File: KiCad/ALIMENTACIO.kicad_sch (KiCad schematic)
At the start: 17 parts, among them J1 Conn_01x02_Pin, U1 LM2596S-5, U2 LM1117DT-3.3

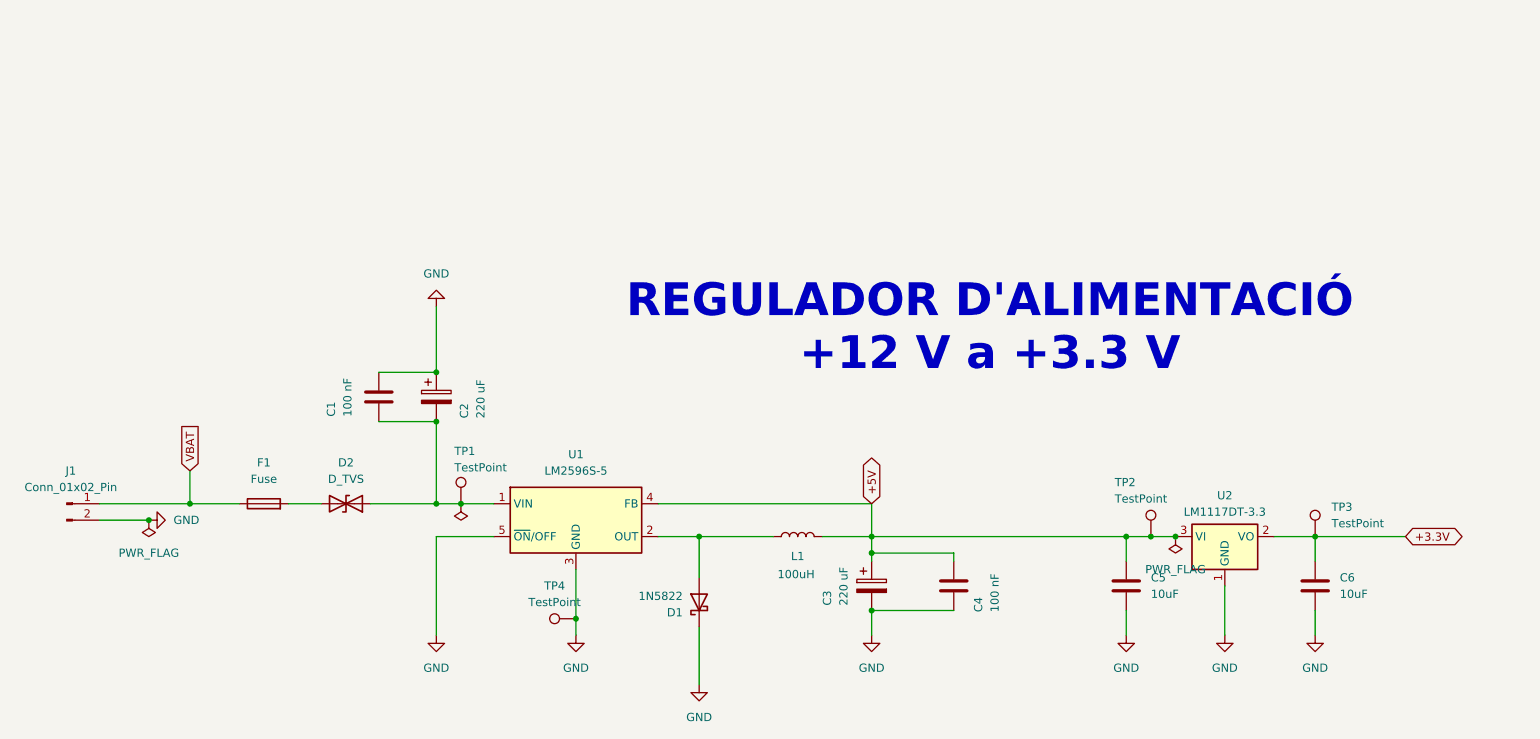
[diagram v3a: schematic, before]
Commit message: Modificació d'errors varis
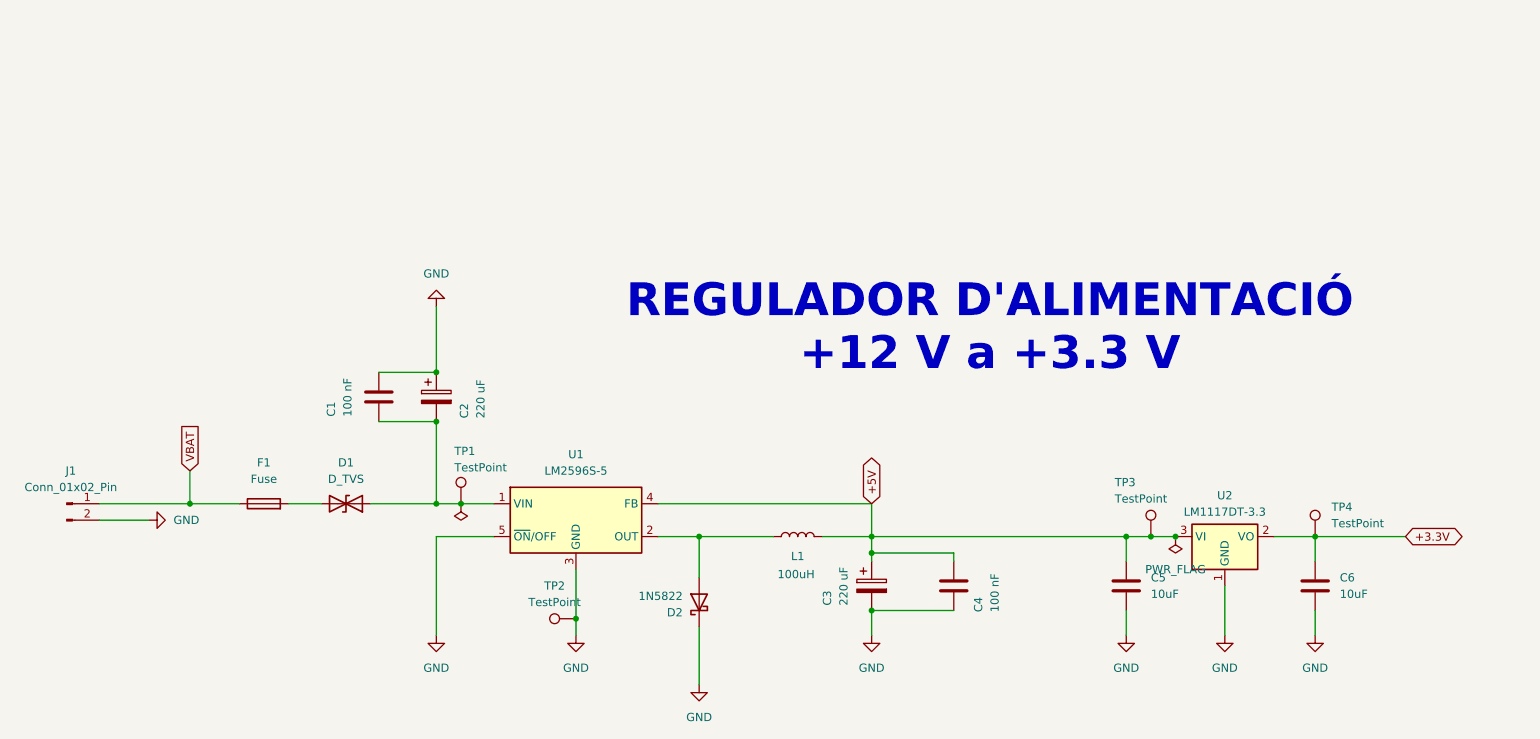
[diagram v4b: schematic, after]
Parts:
- renumbered D2 to D1, D1 to D2, TP4 to TP2, TP2 to TP3, TP3 to TP4
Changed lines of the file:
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@@
-	)
-	(junction
-		(at 55.88 109.22)
-		(diameter 0)
-		(color 0 0 0 0)
 	)
 	(junction
@@
 		(dnp no)
 		(fields_autoplaced yes)
-		(property "Reference" "TP4"
+		(property "Reference" "TP2"
 			(at 118.618 119.38 90)
 			(effects
@@
 		(dnp no)
 		(fields_autoplaced yes)
-		(property "Reference" "D2"
+		(property "Reference" "D1"
 			(at 86.36 100.33 0)
 			(effects
@@
 		(dnp no)
 		(fields_autoplaced yes)
-		(property "Reference" "TP3"
+		(property "Reference" "TP4"
 			(at 238.76 107.1879 0)
 			(effects
@@
 		(dnp no)
 		(fields_autoplaced yes)
-		(property "Reference" "#PWR05"
+		(property "Reference" "#PWR06"
 			(at 167.64 133.35 0)
 			(effects
@@
 		(dnp no)
 		(fields_autoplaced yes)
-		(property "Reference" "D1"
+		(property "Reference" "D2"
 			(at 138.43 123.5076 90)
 			(effects
@@
 		(dnp no)
 		(fields_autoplaced yes)
-		(property "Reference" "#PWR02"
+		(property "Reference" "#PWR03"
 			(at 100.33 133.35 0)
 			(effects
@@
 		(dnp no)
 		(fields_autoplaced yes)
-		(property "Reference" "#PWR08"
+		(property "Reference" "#PWR09"
 			(at 236.22 133.35 0)
 			(effects
@@
 		(dnp no)
 		(fields_autoplaced yes)
-		(property "Reference" "#PWR07"
+		(property "Reference" "#PWR08"
 			(at 222.25 133.35 0)
 			(effects
@@
 		(dnp no)
 		(fields_autoplaced yes)
-		(property "Reference" "#PWR03"
+		(property "Reference" "#PWR04"
 			(at 121.92 133.35 0)
 			(effects
@@
 		(on_board yes)
 		(dnp no)
-		(property "Reference" "TP2"
+		(property "Reference" "TP3"
 			(at 205.232 103.378 0)
 			(effects
@@
 		(dnp no)
 		(fields_autoplaced yes)
-		(property "Reference" "#PWR06"
+		(property "Reference" "#PWR07"
 			(at 207.01 133.35 0)
 			(effects
@@
 		(dnp no)
 		(fields_autoplaced yes)
-		(property "Reference" "#FLG03"
+		(property "Reference" "#FLG0104"
 			(at 214.63 113.665 0)
 			(effects
@@
 				)
 			)
+			(project "SEIENTS_EDD"
+				(path "/b6401b4f-5426-49b8-bb2e-8ecdb19989ef/67d546eb-b5d9-4a2c-a3ee-41df96785a31"
+					(reference "#FLG0104")
+					(unit 1)
+				)
+			)
 		)
 	)
@@
 		(dnp no)
 		(fields_autoplaced yes)
-		(property "Reference" "#PWR04"
+		(property "Reference" "#PWR05"
 			(at 140.97 140.97 0)
 			(effects
@@
 	(symbol
 		(lib_id "power:PWR_FLAG")
-		(at 55.88 109.22 180)
+		(at 104.14 106.68 180)
 		(unit 1)
 		(exclude_from_sim no)
@@
 		(dnp no)
 		(fields_autoplaced yes)
-		(property "Reference" "#FLG02"
-			(at 55.88 111.125 0)
-			(effects
-				(font
-					(size 1.27 1.27)
-				)
-				(hide yes)
-			)
-		)
-		(property "Value" "PWR_FLAG"
-			(at 55.88 114.3 0)
-			(effects
-				(font
-					(size 1.27 1.27)
-				)
-			)
-		)
-		(property "Footprint" ""
-			(at 55.88 109.22 0)
-			(effects
-				(font
-					(size 1.27 1.27)
-				)
-				(hide yes)
-			)
-		)
-		(property "Datasheet" "~"
-			(at 55.88 109.22 0)
-			(effects
-				(font
-					(size 1.27 1.27)
-				)
-				(hide yes)
-			)
-		)
-		(property "Description" "Special symbol for telling ERC where power comes from"
-			(at 55.88 109.22 0)
-			(effects
-				(font
-					(size 1.27 1.27)
-				)
-				(hide yes)
-			)
-		)
-		(pin "1"
-		)
-		(instances
-			(project ""
-				(path "/45cfcaa5-e694-40cb-923c-70f0cad76365"
-					(reference "#FLG02")
-					(unit 1)
-				)
-			)
-		)
-	)
-	(symbol
-		(lib_id "power:PWR_FLAG")
-		(at 104.14 106.68 180)
-		(unit 1)
-		(exclude_from_sim no)
-		(in_bom yes)
-		(on_board yes)
-		(dnp no)
-		(fields_autoplaced yes)
-		(property "Reference" "#FLG01"
+		(property "Reference" "#FLG03"
 			(at 104.14 108.585 0)
 			(effects
@@
 		(dnp no)
 		(fields_autoplaced yes)
-		(property "Reference" "#PWR09"
+		(property "Reference" "#PWR02"
 			(at 100.33 69.85 0)
 			(effects

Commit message: cambios en organizacion
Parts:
- renumbered D2 to D1, D1 to D2, TP3 to TP2, TP4 to TP3, TP2 to TP4
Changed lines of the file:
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@@
 	(text "REGULADOR D'ALIMENTACIÓ\n+12 V a +3.3 V"
 		(exclude_from_sim no)
-		(at 185.928 79.502 0)
+		(at 138.684 53.848 0)
 		(effects
 			(font
+				(face "Arial Black")
 				(size 5.08 5.08)
 				(thickness 0.254)
@@
 		(dnp no)
 		(fields_autoplaced yes)
-		(property "Reference" "TP2"
+		(property "Reference" "TP4"
 			(at 118.618 119.38 90)
 			(effects
@@
 		(dnp no)
 		(fields_autoplaced yes)
-		(property "Reference" "D1"
+		(property "Reference" "D2"
 			(at 86.36 100.33 0)
 			(effects
@@
 		(dnp no)
 		(fields_autoplaced yes)
-		(property "Reference" "TP4"
+		(property "Reference" "TP3"
 			(at 238.76 107.1879 0)
 			(effects
@@
 		(dnp no)
 		(fields_autoplaced yes)
-		(property "Reference" "#PWR06"
+		(property "Reference" "#PWR05"
 			(at 167.64 133.35 0)
 			(effects
@@
 		(dnp no)
 		(fields_autoplaced yes)
-		(property "Reference" "D2"
+		(property "Reference" "D1"
 			(at 138.43 123.5076 90)
 			(effects
@@
 		(dnp no)
 		(fields_autoplaced yes)
-		(property "Reference" "#PWR03"
+		(property "Reference" "#PWR02"
 			(at 100.33 133.35 0)
 			(effects
@@
 		(dnp no)
 		(fields_autoplaced yes)
-		(property "Reference" "#PWR09"
+		(property "Reference" "#PWR08"
 			(at 236.22 133.35 0)
 			(effects
@@
 		(dnp no)
 		(fields_autoplaced yes)
-		(property "Reference" "#PWR08"
+		(property "Reference" "#PWR07"
 			(at 222.25 133.35 0)
 			(effects
@@
 		(dnp no)
 		(fields_autoplaced yes)
-		(property "Reference" "#PWR04"
+		(property "Reference" "#PWR03"
 			(at 121.92 133.35 0)
 			(effects
@@
 		(on_board yes)
 		(dnp no)
-		(property "Reference" "TP3"
+		(property "Reference" "TP2"
 			(at 205.232 103.378 0)
 			(effects
@@
 		(dnp no)
 		(fields_autoplaced yes)
-		(property "Reference" "#PWR07"
+		(property "Reference" "#PWR06"
 			(at 207.01 133.35 0)
 			(effects
@@
 		(dnp no)
 		(fields_autoplaced yes)
-		(property "Reference" "#FLG0104"
+		(property "Reference" "#FLG03"
 			(at 214.63 113.665 0)
 			(effects
@@
 		(dnp no)
 		(fields_autoplaced yes)
-		(property "Reference" "#PWR05"
+		(property "Reference" "#PWR04"
 			(at 140.97 140.97 0)
 			(effects
@@
 		(dnp no)
 		(fields_autoplaced yes)
-		(property "Reference" "#FLG03"
+		(property "Reference" "#FLG01"
 			(at 104.14 108.585 0)
 			(effects
@@
 		(dnp no)
 		(fields_autoplaced yes)
-		(property "Reference" "#PWR02"
+		(property "Reference" "#PWR09"
 			(at 100.33 69.85 0)
 			(effects

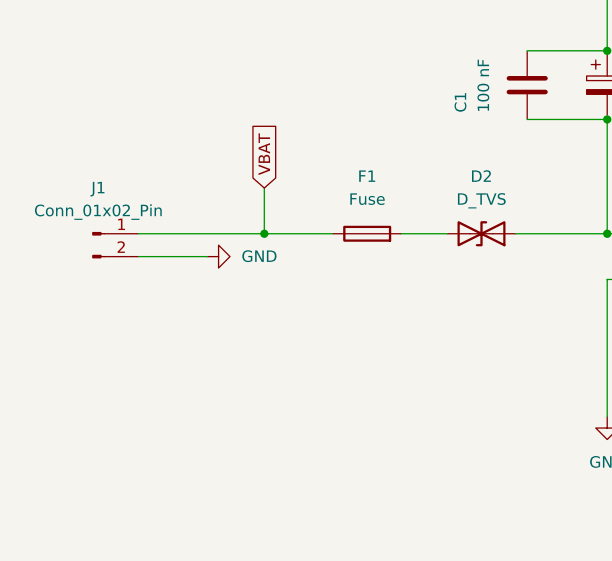
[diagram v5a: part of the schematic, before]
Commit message: Modificació d'errors varis
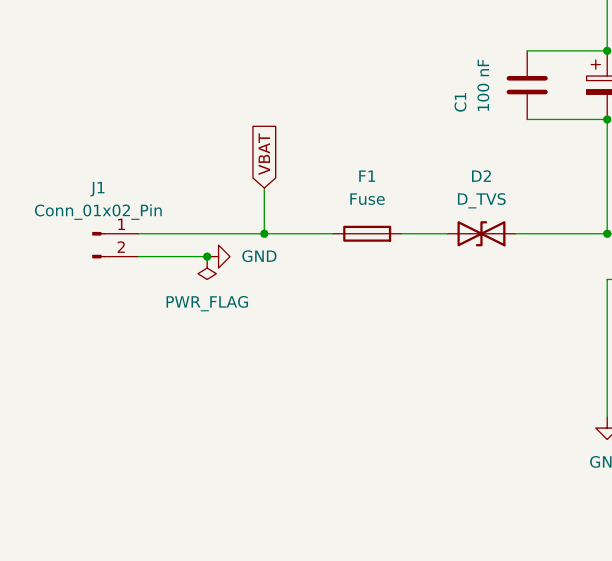
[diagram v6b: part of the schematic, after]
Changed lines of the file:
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@@
+	)
+	(junction
+		(at 55.88 109.22)
+		(diameter 0)
+		(color 0 0 0 0)
 	)
 	(junction
@@
 					(unit 1)
 				)
+			)
+		)
+	)
+	(symbol
+		(lib_id "power:PWR_FLAG")
+		(at 55.88 109.22 180)
+		(unit 1)
+		(exclude_from_sim no)
+		(in_bom yes)
+		(on_board yes)
+		(dnp no)
+		(fields_autoplaced yes)
+		(property "Reference" "#FLG02"
+			(at 55.88 111.125 0)
+			(effects
+				(font
+					(size 1.27 1.27)
+				)
+				(hide yes)
+			)
+		)
+		(property "Value" "PWR_FLAG"
+			(at 55.88 114.3 0)
+			(effects
+				(font
+					(size 1.27 1.27)
+				)
+			)
+		)
+		(property "Footprint" ""
+			(at 55.88 109.22 0)
+			(effects
+				(font
+					(size 1.27 1.27)
+				)
+				(hide yes)
+			)
+		)
+		(property "Datasheet" "~"
+			(at 55.88 109.22 0)
+			(effects
+				(font
+					(size 1.27 1.27)
+				)
+				(hide yes)
+			)
+		)
+		(property "Description" "Special symbol for telling ERC where power comes from"
+			(at 55.88 109.22 0)
+			(effects
+				(font
+					(size 1.27 1.27)
+				)
+				(hide yes)
+			)
+		)
+		(pin "1"
+		)
+		(instances
+			(project "ALIMENTACIO"
+				(path "/45cfcaa5-e694-40cb-923c-70f0cad76365"
+					(reference "#FLG02")
+					(unit 1)
+				)

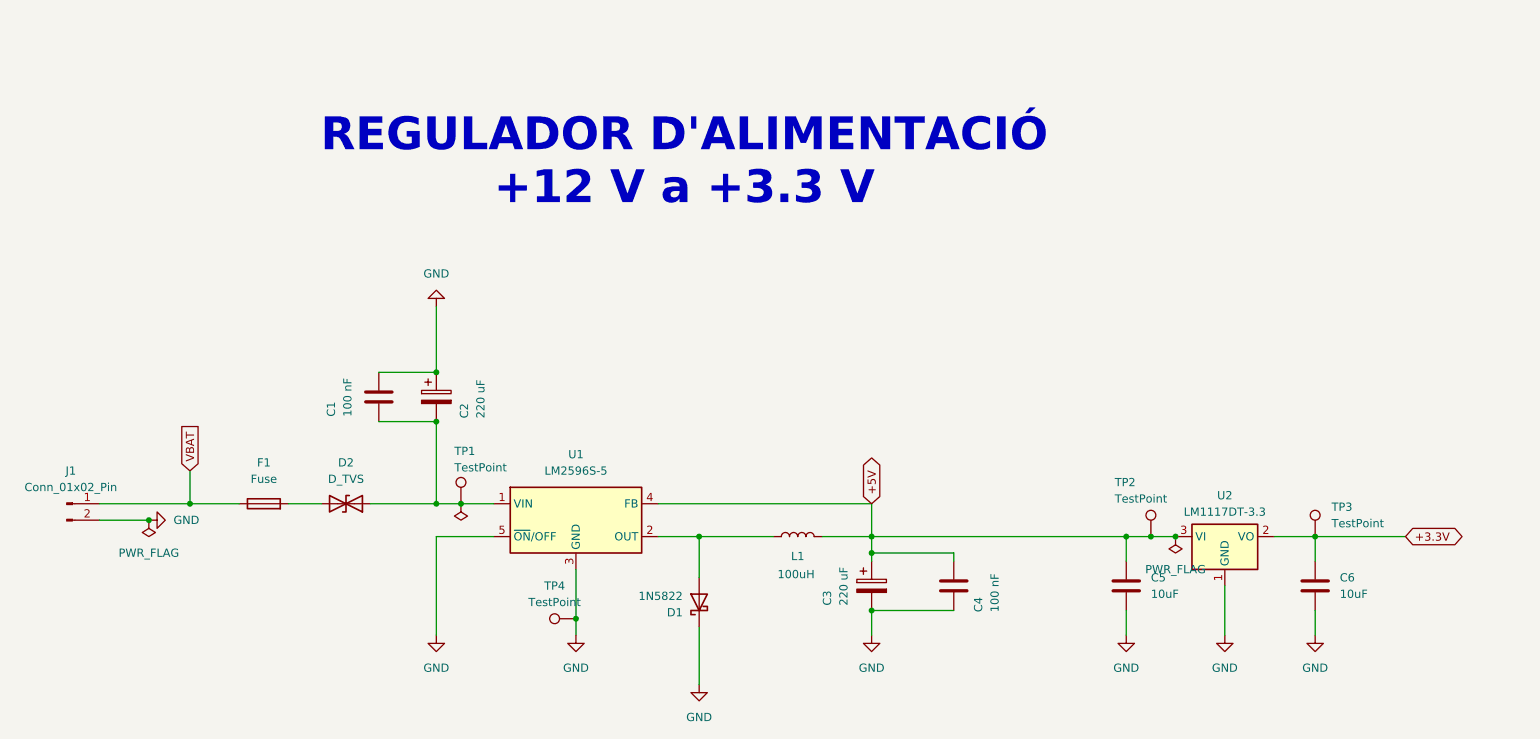
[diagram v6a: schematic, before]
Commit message: Modificació d'errors varis
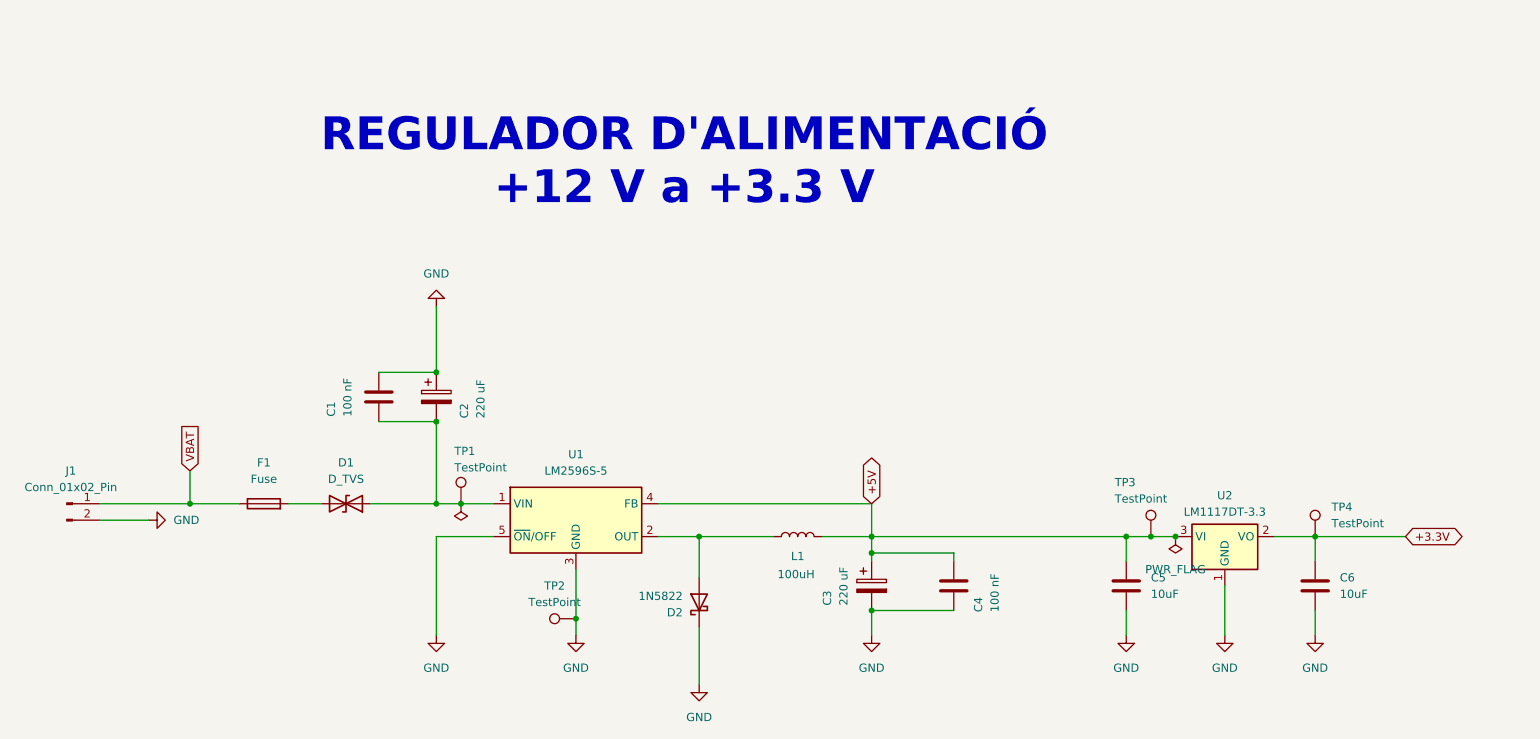
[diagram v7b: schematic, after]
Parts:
- renumbered D2 to D1, D1 to D2, TP4 to TP2, TP2 to TP3, TP3 to TP4
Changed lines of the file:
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@@
-	)
-	(junction
-		(at 55.88 109.22)
-		(diameter 0)
-		(color 0 0 0 0)
 	)
 	(junction
@@
 		(dnp no)
 		(fields_autoplaced yes)
-		(property "Reference" "TP4"
+		(property "Reference" "TP2"
 			(at 118.618 119.38 90)
 			(effects
@@
 		(dnp no)
 		(fields_autoplaced yes)
-		(property "Reference" "D2"
+		(property "Reference" "D1"
 			(at 86.36 100.33 0)
 			(effects
@@
 		(dnp no)
 		(fields_autoplaced yes)
-		(property "Reference" "TP3"
+		(property "Reference" "TP4"
 			(at 238.76 107.1879 0)
 			(effects
@@
 		(dnp no)
 		(fields_autoplaced yes)
-		(property "Reference" "#PWR05"
+		(property "Reference" "#PWR06"
 			(at 167.64 133.35 0)
 			(effects
@@
 		(dnp no)
 		(fields_autoplaced yes)
-		(property "Reference" "D1"
+		(property "Reference" "D2"
 			(at 138.43 123.5076 90)
 			(effects
@@
 		(dnp no)
 		(fields_autoplaced yes)
-		(property "Reference" "#PWR02"
+		(property "Reference" "#PWR03"
 			(at 100.33 133.35 0)
 			(effects
@@
 		(dnp no)
 		(fields_autoplaced yes)
-		(property "Reference" "#PWR08"
+		(property "Reference" "#PWR09"
 			(at 236.22 133.35 0)
 			(effects
@@
 		(dnp no)
 		(fields_autoplaced yes)
-		(property "Reference" "#PWR07"
+		(property "Reference" "#PWR08"
 			(at 222.25 133.35 0)
 			(effects
@@
 		(dnp no)
 		(fields_autoplaced yes)
-		(property "Reference" "#PWR03"
+		(property "Reference" "#PWR04"
 			(at 121.92 133.35 0)
 			(effects
@@
 	)
 	(symbol
-		(lib_id "power:PWR_FLAG")
-		(at 55.88 109.22 180)
-		(unit 1)
-		(exclude_from_sim no)
-		(in_bom yes)
-		(on_board yes)
-		(dnp no)
-		(fields_autoplaced yes)
-		(property "Reference" "#FLG02"
-			(at 55.88 111.125 0)
-			(effects
-				(font
-					(size 1.27 1.27)
-				)
-				(hide yes)
-			)
-		)
-		(property "Value" "PWR_FLAG"
-			(at 55.88 114.3 0)
-			(effects
-				(font
-					(size 1.27 1.27)
-				)
-			)
-		)
-		(property "Footprint" ""
-			(at 55.88 109.22 0)
-			(effects
-				(font
-					(size 1.27 1.27)
-				)
-				(hide yes)
-			)
-		)
-		(property "Datasheet" "~"
-			(at 55.88 109.22 0)
-			(effects
-				(font
-					(size 1.27 1.27)
-				)
-				(hide yes)
-			)
-		)
-		(property "Description" "Special symbol for telling ERC where power comes from"
-			(at 55.88 109.22 0)
-			(effects
-				(font
-					(size 1.27 1.27)
-				)
-				(hide yes)
-			)
-		)
-		(pin "1"
-		)
-		(instances
-			(project "ALIMENTACIO"
-				(path "/45cfcaa5-e694-40cb-923c-70f0cad76365"
-					(reference "#FLG02")
-					(unit 1)
-				)
-			)
-		)
-	)
-	(symbol
 		(lib_id "Device:C")
 		(at 180.34 119.38 0)
@@
 		(on_board yes)
 		(dnp no)
-		(property "Reference" "TP2"
+		(property "Reference" "TP3"
 			(at 205.232 103.378 0)
 			(effects
@@
 		(dnp no)
 		(fields_autoplaced yes)
-		(property "Reference" "#PWR06"
+		(property "Reference" "#PWR07"
 			(at 207.01 133.35 0)
 			(effects
@@
 		(dnp no)
 		(fields_autoplaced yes)
-		(property "Reference" "#FLG03"
+		(property "Reference" "#FLG0104"
 			(at 214.63 113.665 0)
 			(effects
@@
 		(dnp no)
 		(fields_autoplaced yes)
-		(property "Reference" "#PWR04"
+		(property "Reference" "#PWR05"
 			(at 140.97 140.97 0)
 			(effects
@@
 		(dnp no)
 		(fields_autoplaced yes)
-		(property "Reference" "#FLG01"
+		(property "Reference" "#FLG03"
 			(at 104.14 108.585 0)
 			(effects
@@
 		(dnp no)
 		(fields_autoplaced yes)
-		(property "Reference" "#PWR09"
+		(property "Reference" "#PWR02"
 			(at 100.33 69.85 0)
 			(effects

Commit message: FootPrints Canviats
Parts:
- J1: footprint Connector_PinHeader_2.54mm:PinHeader_1x02_P2.54mm_Vertical -> TerminalBlock_Phoenix:TerminalBlock_Phoenix_MKDS-1,5-2-5.08_1x02_P5.08mm_Horizontal
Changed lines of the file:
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@@
 			)
 		)
-		(property "Footprint" "Connector_PinHeader_2.54mm:PinHeader_1x02_P2.54mm_Vertical"
+		(property "Footprint" "TerminalBlock_Phoenix:TerminalBlock_Phoenix_MKDS-1,5-2-5.08_1x02_P5.08mm_Horizontal"
 			(at 43.18 106.68 0)
 			(effects
